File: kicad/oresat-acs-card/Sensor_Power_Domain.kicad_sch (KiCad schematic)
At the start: 79 parts, among them Q26 MOSFET-PCH-SOT23-6, Q27 MOSFET-PCH-SOT23-6, Q28 PMV45EN2R, Q29 PMV45EN2R, Q30 MOSFET-PCH-dual-SOT23-6, U29 MAX7310ATE, U30 MAX4211FETE, U31 TPS62111RSA, U32 MIC842LYC5-TR, U33 MIC842LYC5-TR

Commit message: Updated 5 V regulator and tweaked card layout. Cleaned up silkscreen layer and schematic.
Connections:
- net PB6/SCL renamed PB6/SCL
- net PB7/SDA renamed PB7/SDA
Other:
- moved on the sheet: C43, C44, C45, C46, C47, C48, C49, C50, D16, D17, D18, L3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

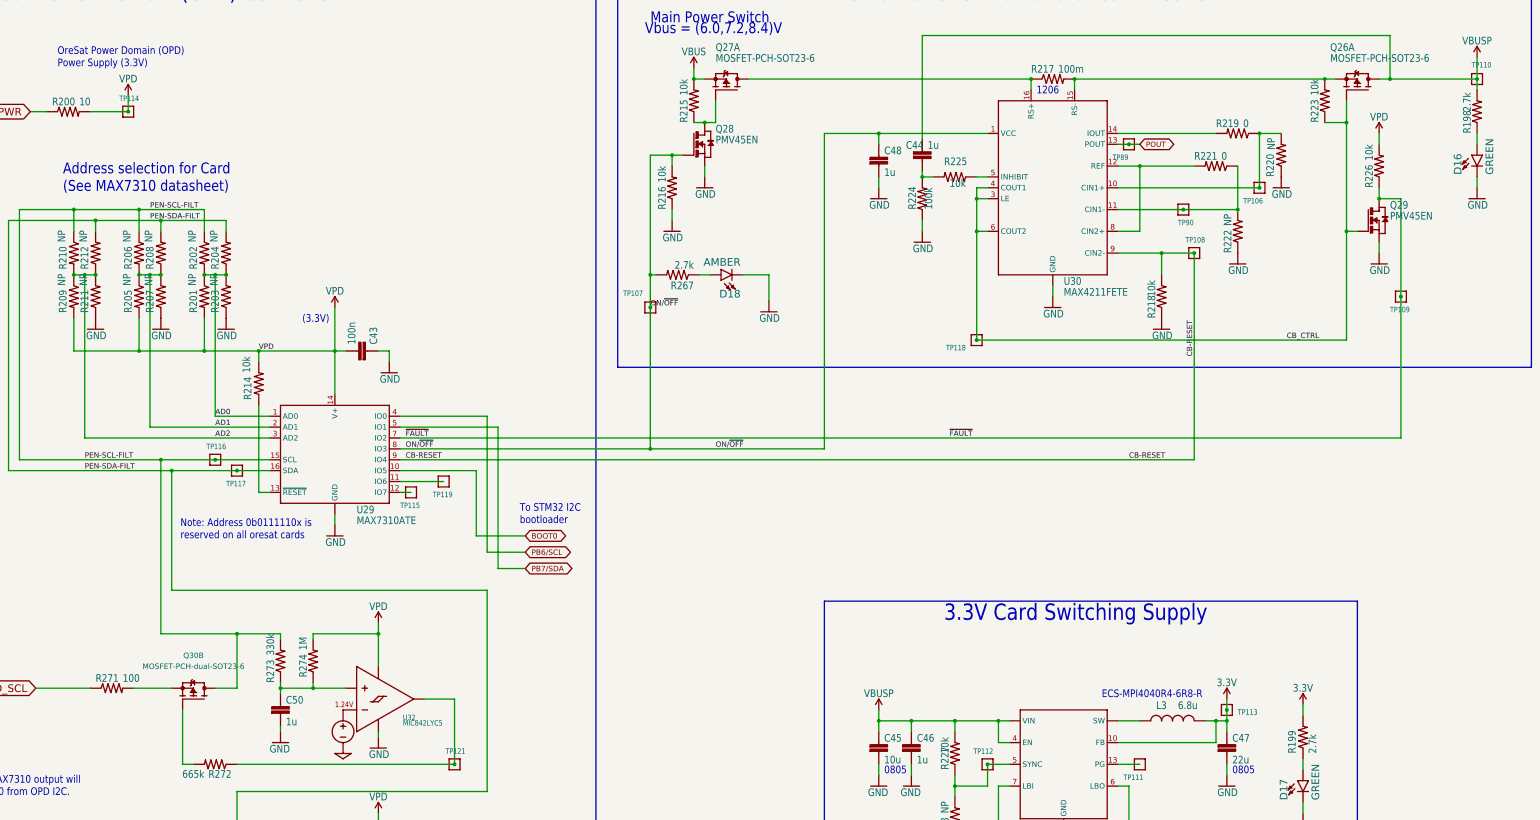
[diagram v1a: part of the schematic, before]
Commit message: Updated 5V regulators to match design block. Added UART switch to microcontroller. Added power flags and cleaned up ERC errors
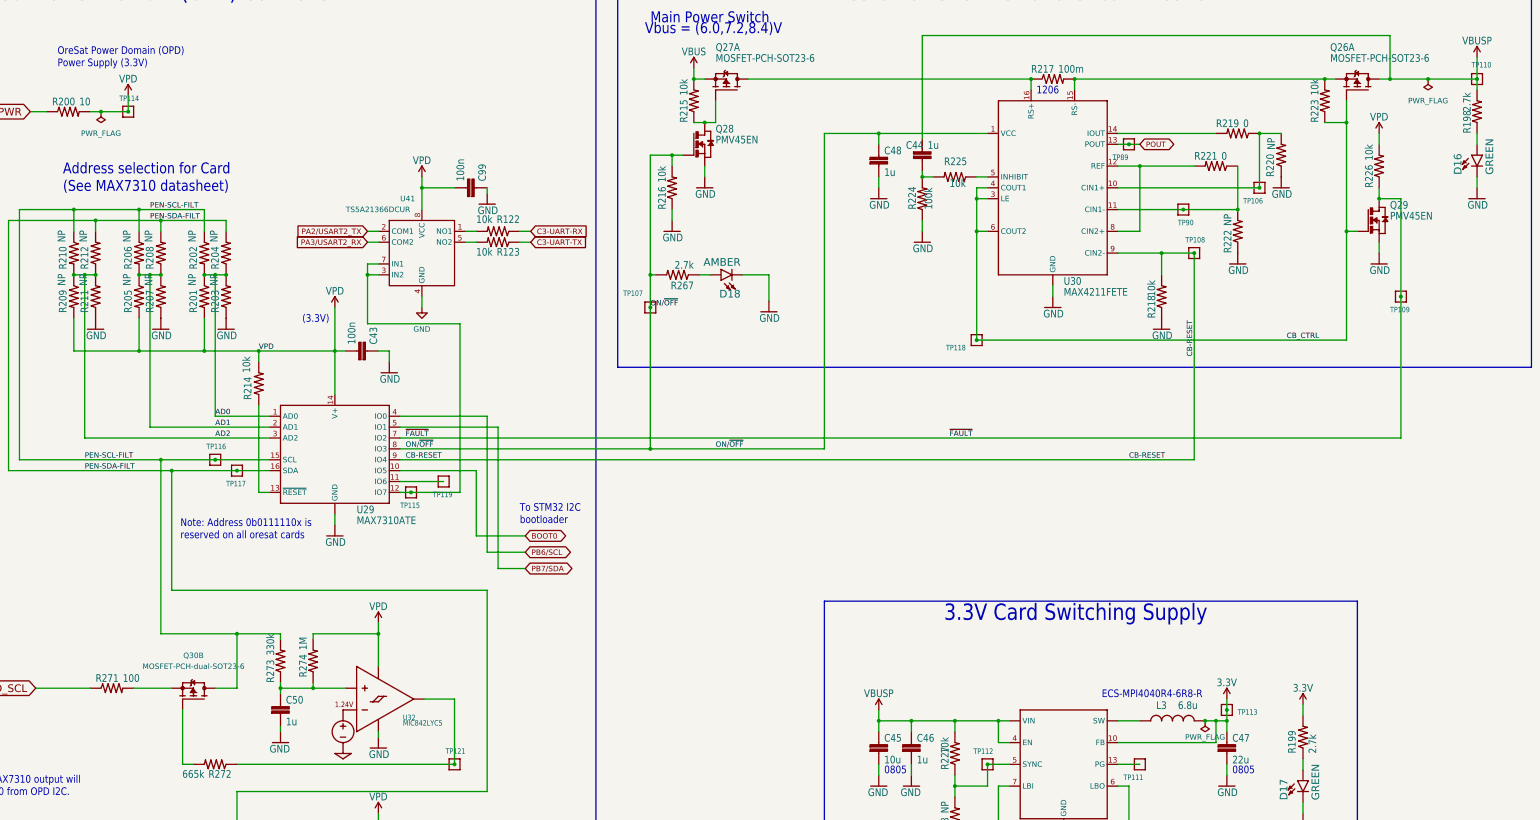
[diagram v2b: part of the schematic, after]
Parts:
- added C99: CL10B104KB8NNNL, oresat-acs-card:.0603-C-NOSILK, symbol oresat-acs-card-eagle-import:C-EU0603-C-NOSILK
- added R122, R123: RC0603FR-0710KL, oresat-acs-card:.0603-C-NOSILK, symbol oresat-acs-card-eagle-import:R-US_0603-C-NOSILK
- added U41: TS5A21366DCUR, oresat-acs-card:DCU-R-PDSO-G8, symbol oresat-acs-card-eagle-import:TS5A21366DCUR
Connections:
- net GND: now also C99.1, U41.4 (GND)
- net VPD: now also C99.2, U41.8 (VCC)
- net at TP115.1, U29.12 (IO7): now also U41.3 (IN2), U41.7 (IN1)
- new net: R123.2, U41.5 (NO2)
- new net: R122.2, U41.1 (NO1)
- new net C3-UART-RX: R122.1
- new net C3-UART-TX: R123.1
- new net PA2/USART2_TX: U41.2 (COM1)
- new net PA3/USART2_RX: U41.6 (COM2)

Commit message: Design review changes.
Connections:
- net ON/~{OFF}: now also C99.2, U41.8 (VCC)
- net VPD: no longer C99.2, U41.8 (VCC)
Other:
- note added: "Resistor values TBD"
- note added: "Should allow enough current to run magnetorquers (0.6 A max each, 1.8 A total)"
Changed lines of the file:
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@@
   (junction (at 204.47 91.44) (diameter 0) (color 0 0 0 0)
   )
+  (junction (at 204.47 55.88) (diameter 0) (color 0 0 0 0)
+  )
   (wire (pts (xy 166.37 204.47) (xy 166.37 157.48))
     (stroke (width 0) (type default) (color 0 0 0 0))
@@
     (stroke (width 0) (type default) (color 0 0 0 0))
   )
+  (wire (pts (xy 204.47 55.88) (xy 151.13 55.88))
+    (stroke (width 0) (type default) (color 0 0 0 0))
+  )
   (wire (pts (xy 336.55 187.96) (xy 334.01 187.96))
     (stroke (width 0) (type default) (color 0 0 0 0))
@@
     (stroke (width 0) (type default) (color 0 0 0 0))
   )
-  (wire (pts (xy 151.13 60.96) (xy 151.13 63.5))
+  (wire (pts (xy 151.13 55.88) (xy 151.13 63.5))
     (stroke (width 0) (type default) (color 0 0 0 0))
   )
@@
     (effects (font (size 1.778 1.5113)) (justify left bottom))
   )
-  (text "3.3V Card Switching Supply" (at 273.05 165.1 180)
+  (text "3.3V Card Switching Supply" (at 273.05 170.18 180)
     (effects (font (size 3.81 3.2385)) (justify left bottom))
   )
   (text "ECS-MPI4040R4-6R8-R" (at 309.88 182.88 180)
     (effects (font (size 1.778 1.5113)) (justify left bottom))
+  )
+  (text "Should allow enough current to run magnetorquers\n(0.6 A max each, 1.8 A total)"
+    (at 308.61 35.56 0)
+    (effects (font (size 1.27 1.27)) (justify left bottom))
   )
   (text "OreSat Power Domain (OPD)\nPower Supply (3.3V)" (at 66.04 35.56 180)
@@
     (effects (font (size 1.778 1.5113)) (justify left bottom))
   )
+  (text "Resistor values TBD" (at 314.96 46.99 0)
+    (effects (font (size 1.27 1.27)) (justify left bottom))
+  )
   (text "Address selection for Card\n(See MAX7310 datasheet)"
     (at 67.31 64.77 0)
@@
     (effects (font (size 1.778 1.5113)) (justify left bottom))
   )
-  (text "Main Power Switch" (at 204.47 25.4 180)
+  (text "Main Power Switch" (at 204.47 24.13 180)
     (effects (font (size 2.54 2.159)) (justify left bottom))
   )
@@
     (effects (font (size 1.2446 1.2446)) (justify left bottom))
   )
+  (label "ON/~{OFF}" (at 151.13 55.88 0)
+    (effects (font (size 1.2446 1.2446)) (justify left bottom))
+  )
   (label "PEN-SCL-FILT" (at 72.39 127 0)
     (effects (font (size 1.2446 1.2446)) (justify left bottom))
@@
     (effects (font (size 1.2446 1.2446)) (justify left bottom))
   )
+  (label "ON/~{OFF}" (at 246.38 50.8 0)
+    (effects (font (size 1.2446 1.2446)) (justify left bottom))
+  )
   (label "CB-RESET" (at 316.23 127 0)
     (effects (font (size 1.2446 1.2446)) (justify left bottom))
   )
   (label "PEN-SDA-FILT" (at 72.39 129.54 0)
+    (effects (font (size 1.2446 1.2446)) (justify left bottom))
+  )
+  (label "ON/~{OFF}" (at 204.47 64.77 90)
     (effects (font (size 1.2446 1.2446)) (justify left bottom))
   )
@@
     (pin "2")
   )
-  (symbol (lib_id "oresat-acs-card-eagle-import:VPD") (at 151.13 60.96 0) (unit 1)
-    (in_bom yes) (on_board yes)
-    (property "Reference" "#VPD01" (id 0) (at 151.13 60.96 0)
-      (effects (font (size 1.27 1.27)) hide)
-    )
-    (property "Value" "VPD" (id 1) (at 151.13 58.166 0)
-      (effects (font (size 1.778 1.5113)) (justify bottom))
-    )
-    (property "Footprint" "" (id 2) (at 151.13 60.96 0)
-      (effects (font (size 1.27 1.27)) hide)
-    )
-    (property "Datasheet" "" (id 3) (at 151.13 60.96 0)
-      (effects (font (size 1.27 1.27)) hide)
-    )
-    (pin "1")
-  )
   (symbol (lib_id "oresat-acs-card-eagle-import:R-US_0603-C-NOSILK") (at 275.59 210.82 90) (unit 1)
     (in_bom yes) (on_board yes)
@@
   (symbol (lib_id "oresat-acs-card-eagle-import:R-US_0603-C-NOSILK") (at 397.51 45.72 90) (unit 1)
     (in_bom yes) (on_board yes)
-    (property "Reference" "R198" (id 0) (at 396.24 50.8 0)
-      (effects (font (size 1.778 1.5113)) (justify left bottom))
-    )
-    (property "Value" "2.7k" (id 1) (at 396.24 45.72 0)
+    (property "Reference" "R198" (id 0) (at 396.24 52.07 0)
+      (effects (font (size 1.778 1.5113)) (justify left bottom))
+    )
+    (property "Value" "10k" (id 1) (at 396.24 45.085 0)
       (effects (font (size 1.778 1.5113)) (justify left bottom))
     )
@@
       (effects (font (size 1.778 1.5113)) (justify left bottom))
     )
-    (property "Value" "2.7k" (id 1) (at 214.63 80.518 0)
+    (property "Value" "4.7k" (id 1) (at 214.63 80.518 0)
       (effects (font (size 1.778 1.5113)) (justify left bottom))
     )
@@
   (symbol (lib_id "oresat-acs-card-eagle-import:R-US_0603-C-NOSILK") (at 323.85 88.9 90) (unit 1)
     (in_bom yes) (on_board yes)
-    (property "Reference" "R218" (id 0) (at 322.58 93.98 0)
+    (property "Reference" "R218" (id 0) (at 322.58 95.25 0)
       (effects (font (size 1.778 1.5113)) (justify left bottom))
     )
@@
   (symbol (lib_id "oresat-acs-card-eagle-import:R-US_0603-C-NOSILK") (at 356.87 191.77 90) (unit 1)
     (in_bom yes) (on_board yes)
-    (property "Reference" "R199" (id 0) (at 355.3714 195.58 0)
-      (effects (font (size 1.778 1.5113)) (justify left bottom))
-    )
-    (property "Value" "2.7k" (id 1) (at 360.172 195.58 0)
-      (effects (font (size 1.778 1.5113)) (justify left bottom))
-    )
+    (property "Reference" "R199" (id 0) (at 355.6 194.945 0)
+      (effects (font (size 1.778 1.5113)) (justify left bottom))
+    )
+    (property "Value" "10k" (id 1) (at 360.68 194.31 0)
+      (effects (font (size 1.778 1.5113)) (justify left bottom))
+    )
